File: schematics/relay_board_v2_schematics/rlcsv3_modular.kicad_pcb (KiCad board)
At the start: 2 copper layers, 45 x 75 mm, 43 parts, among them J1 Programming Header, P1 ACT_PWR, P3 ACTUATOR, Q1 MMBF170, Q2 MMBF170, SW1 SW_DIP_x04, U1 SPST_POWER_RELAY, U2 PIC16F1826-ISO, U3 dpdt_relay, U4 INA180A1, U5 CONN_01x05, U6 INA180A1, U7 CONN_01x05

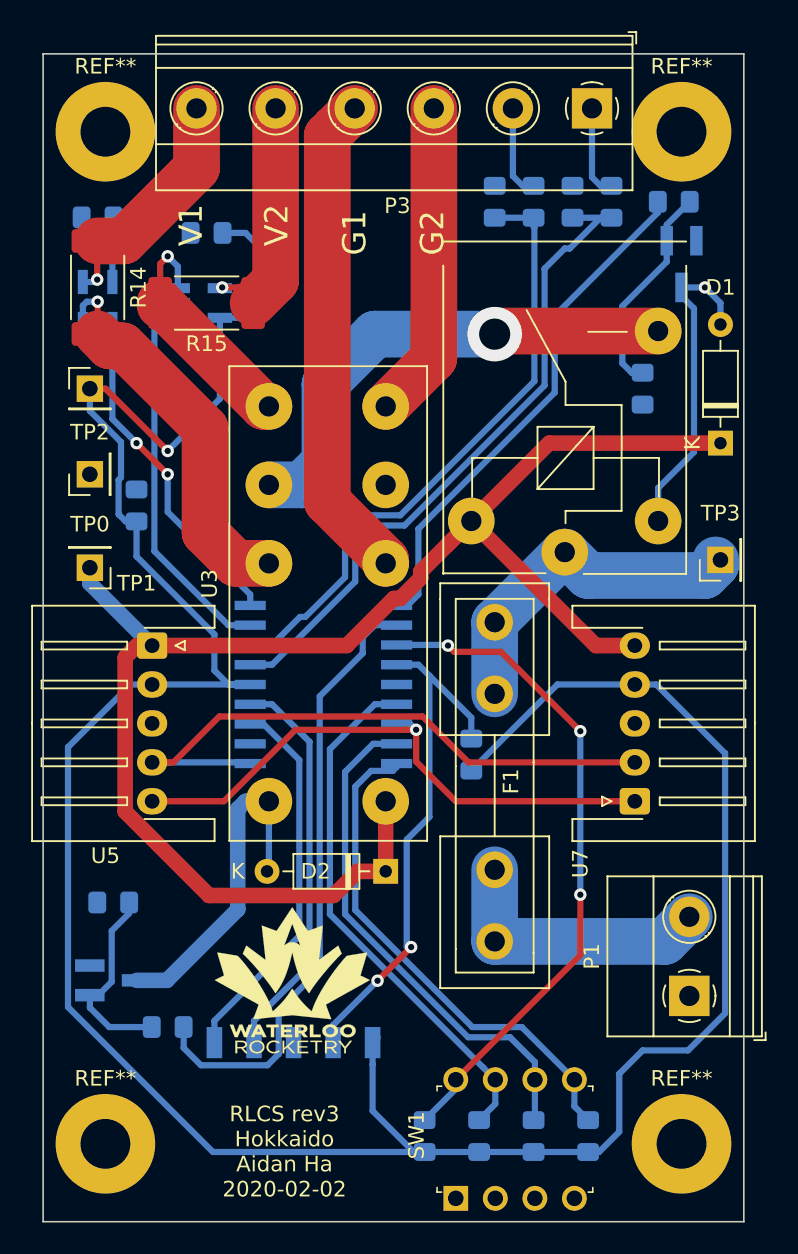
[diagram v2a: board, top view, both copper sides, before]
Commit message: Fix comments, add ground pour and DRC check changes
Signed-off-by: AIDAN HA <qbha@edu.uwaterloo.ca>
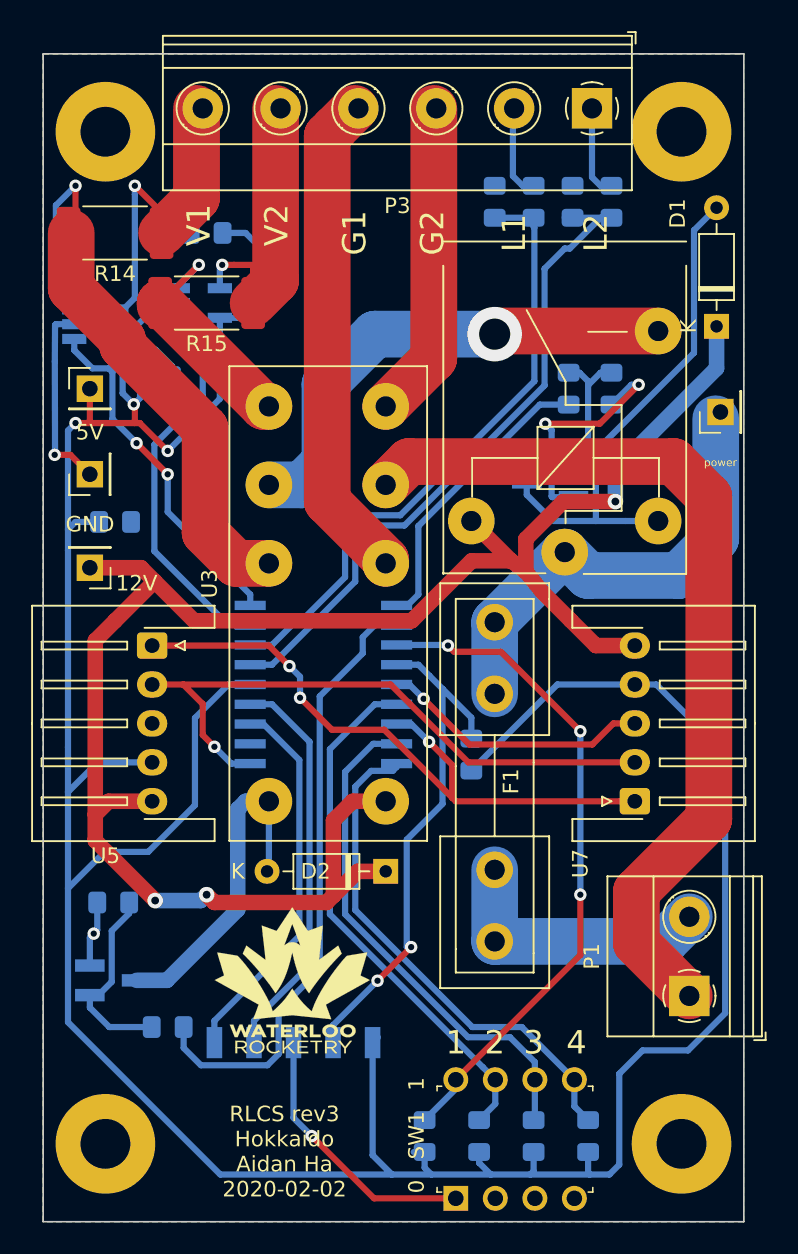
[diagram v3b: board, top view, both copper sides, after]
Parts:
- removed REF** (x2): MountingHole_3.2mm_M3_Pad, MountingHole:MountingHole_3.2mm_M3_Pad
- added ?: MountingHole_3.2mm_M3_Pad, MountingHole:MountingHole_3.2mm_M3_Pad, F.Cu at (134.0, 139.0)
- added ?: MountingHole_3.2mm_M3_Pad, MountingHole:MountingHole_3.2mm_M3_Pad, F.Cu at (171.0, 139.0)
- 0   SW1   1: renamed from SW1
- P3: footprint TerminalBlock_Phoenix:TerminalBlock_Phoenix_MKDS-1,5-6-5.08_1x06_P5.08mm_Horizontal -> TerminalBlock_Phoenix:TerminalBlock_Phoenix_MKDS-1,5-6_1x06_P5.00mm_Horizontal
- moved Q1 16.4 mm to (162.6, 96.5), turned to 180 degrees
- moved R5 13.8 mm to (163.8, 90.5), turned to 270 degrees
- moved C2 10.9 mm to (137.2, 89.8), turned to 180 degrees
- moved power 9.50 mm to (173.5, 92.0)
- moved D1 7.50 mm to (173.2, 86.5)
- moved R14 3.67 mm to (134.6, 80.5), turned to 180 degrees
- moved R11 2.00 mm to (166.5, 90.5)
- moved C1 1.74 mm to (134.6, 99.1), turned to 0 degrees
- moved U4 1.37 mm to (133.3, 86.4), turned to 0 degrees
- renumbered TP1 to 12V, TP2 to 5V, REF** to ?, TP0 to GND, TP3 to power
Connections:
- U2 pad 11: (no net) -> Net-(U2-Pad11)
- U5 pad 1: +12V -> /SDA
- U5 pad 2: +5V -> /SCL
- U5 pad 4: /SCL -> +5V
- U5 pad 5: /SDA -> +12V
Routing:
- net GND: track 0.00 -> 137.1 mm, vias 0 -> 6
- net +5V: track 183.3 -> 211.4 mm, vias 1 -> 3
- net +12V: track 100.8 -> 119.0 mm, vias 0 -> 3
- net Net-(R14-Pad2): track 25.3 -> 40.2 mm
- net /POWER: track 33.3 -> 19.0 mm
- net Net-(D1-Pad2): track 20.6 -> 33.3 mm, vias 1 -> 0
- net Net-(F1-Pad2): track 23.1 -> 31.2 mm
- net /P1: track 15.6 -> 21.4 mm
- net /SDA: track 38.4 -> 43.7 mm, vias 1 -> 3
- net Net-(Q1-Pad1): track 13.7 -> 9.24 mm
- net /P2: track 15.7 -> 19.1 mm
- net /SCL: track 39.9 -> 40.8 mm, vias 0 -> 1
- net /CURR_SENSE_1: track 21.7 -> 22.4 mm
- net /CURR_SENSE_2: track 24.4 -> 25.1 mm
- added copper zone on B.Cu, net GND
- added copper zone on F.Cu, net GND
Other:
- board text added: "1"
- board text added: "2"
- board text added: "3"
- board text added: "4"
- board text added: "L1"
- board text added: "L2"

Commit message: Add round 3 of changes
Signed-off-by: AIDAN HA <qbha@edu.uwaterloo.ca>
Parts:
- added P1: ACT_PWR, TerminalBlock_Phoenix:TerminalBlock_Phoenix_MKDS-1,5-2-5.08_1x02_P5.08mm_Horizontal, F.Cu at (135.0, 123.8)
- moved R12 8.31 mm to (137.5, 131.2)
- moved Q2 7.16 mm to (141.0, 125.5)
- moved R8 2.46 mm to (156.8, 79.5)
- moved R9 2.45 mm to (168.8, 79.5)
- moved R6 2.06 mm to (137.5, 133.5), turned to 180 degrees
- moved P1 1.90 mm to (169.8, 128.8)
- moved U4 1.42 mm to (133.8, 85.0)
- moved R10 1.25 mm to (164.8, 79.5)
- moved R7 1.25 mm to (160.8, 79.5)
- turned C1 to 180 degrees
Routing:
- net GND: track 137.1 -> 190.1 mm
- net Net-(F1-Pad1): track 17.8 -> 50.2 mm
- net +5V: track 211.4 -> 224.9 mm
- net Net-(D2-Pad2): track 23.0 -> 16.1 mm
- net /SDA: track 43.7 -> 39.1 mm
- net /SELECT: track 39.7 -> 43.2 mm
- net Net-(Q2-Pad1): track 12.6 -> 9.28 mm
- net /LIM1: track 39.7 -> 42.8 mm
- net Net-(R14-Pad2): track 40.2 -> 37.6 mm
- net Net-(P3-Pad1): track 5.90 -> 7.81 mm
- net /P1: track 21.4 -> 19.6 mm
- net /~MCLR: track 33.6 -> 34.9 mm
- net /DIP_1: track 43.2 -> 41.9 mm
- net +12V: track 119.0 -> 119.7 mm
- net /CURR_SENSE_1: track 22.4 -> 23.0 mm

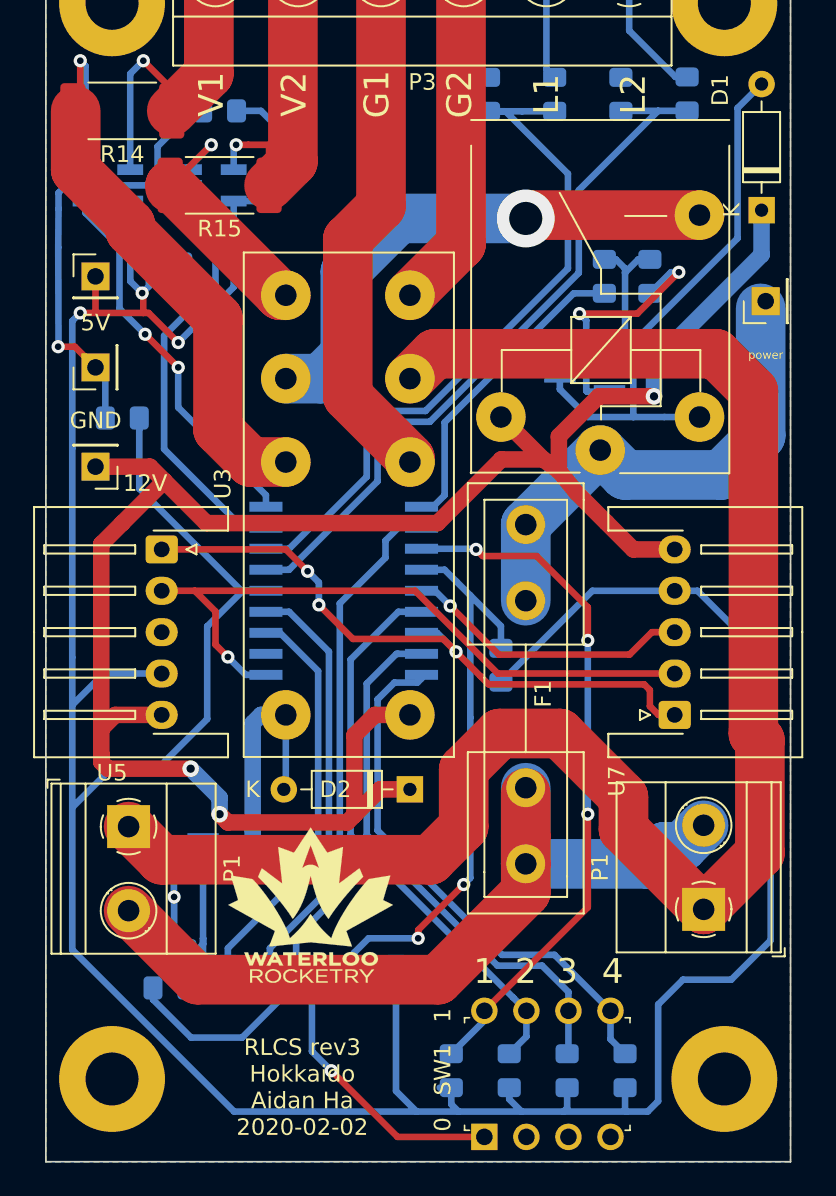
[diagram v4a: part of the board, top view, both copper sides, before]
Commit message: Add final silkscreen changes
Signed-off-by: AIDAN HA <qbha@edu.uwaterloo.ca>
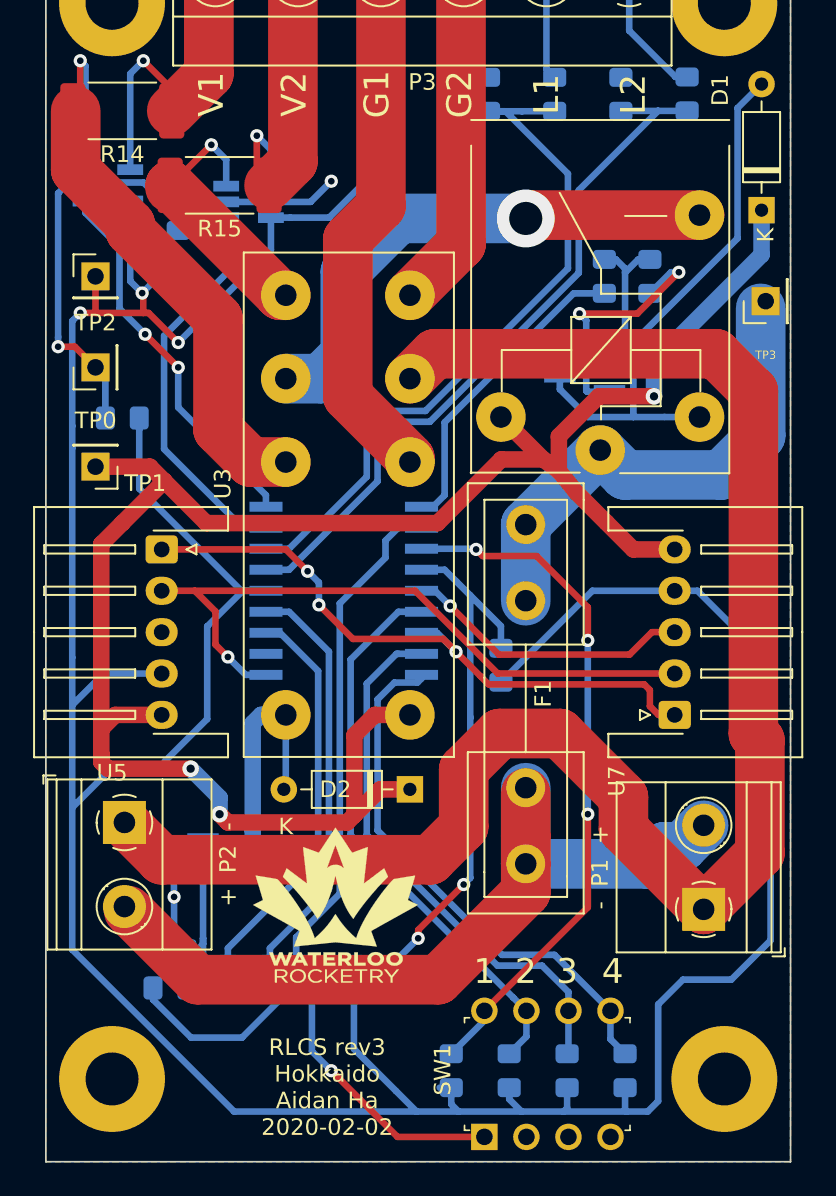
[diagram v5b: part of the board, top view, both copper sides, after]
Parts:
- removed P1: ACT_PWR, TerminalBlock_Phoenix:TerminalBlock_Phoenix_MKDS-1,5-2-5.08_1x02_P5.08mm_Horizontal
- added +  P2  -: ACT_PWR, TerminalBlock_Phoenix:TerminalBlock_Phoenix_MKDS-1,5-2-5.08_1x02_P5.08mm_Horizontal, F.Cu at (134.8, 123.5)
- -  P1  +: renamed from P1
- SW1: renamed from 0   SW1   1
- ~MCLR 5V: renamed from J1
- moved C3 9.33 mm to (149.5, 83.0), turned to 270 degrees
- moved U6 2.46 mm to (142.2, 86.0)
- moved G*** 1.50 mm to (147.5, 128.5)
- moved C2 1.25 mm to (138.0, 88.8), turned to 270 degrees
- renumbered GND to TP0, 12V to TP1, 5V to TP2, power to TP3
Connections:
- ~MCLR 5V pad 4: /~MCLR -> +5V
- ~MCLR 5V pad 5: +5V -> /~MCLR
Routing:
- net /~MCLR: track 34.9 -> 32.1 mm
- net GND: track 190.1 -> 192.1 mm, vias 6 -> 7
- net /CURR_SENSE_2: track 25.1 -> 23.7 mm
- net Net-(R15-Pad2): track 15.5 -> 16.3 mm
- net /P2: track 19.1 -> 19.8 mm

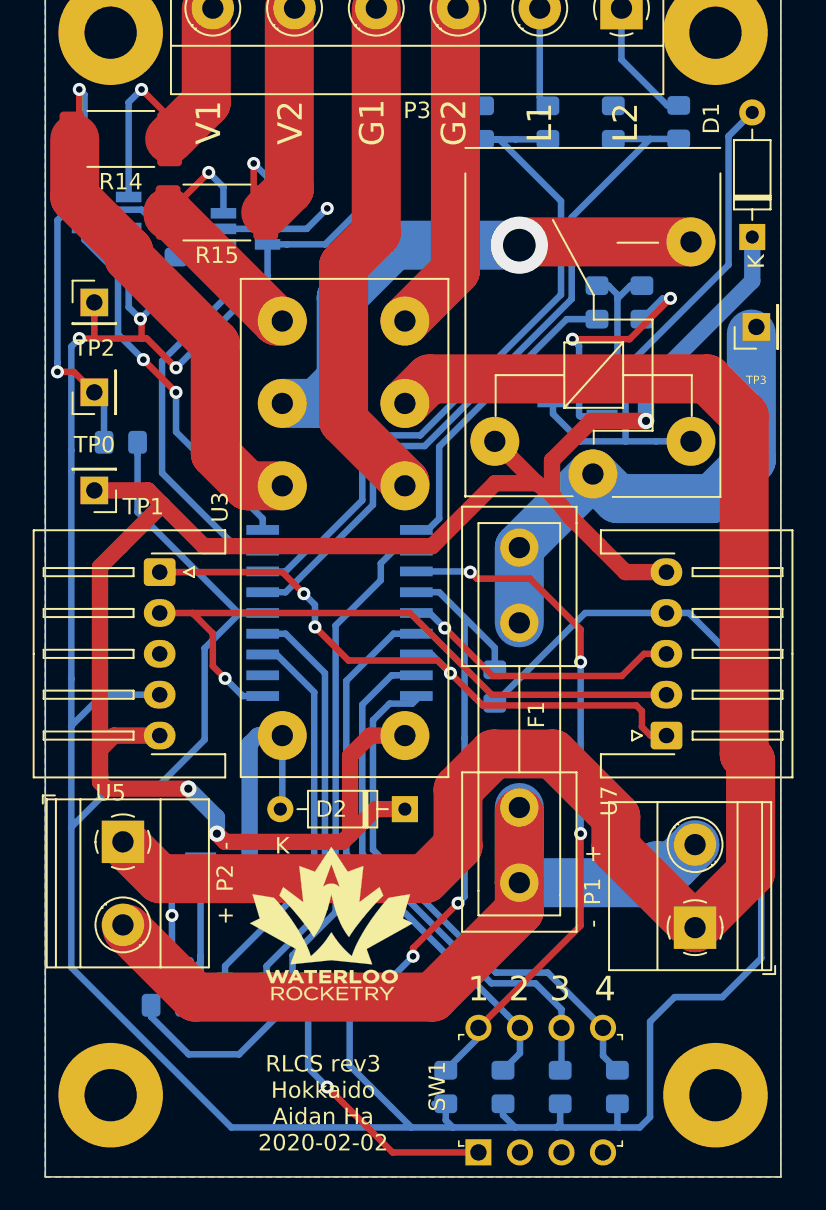
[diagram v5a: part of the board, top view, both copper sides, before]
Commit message: Fix SilkScreen and add Gerbers
Signed-off-by: AIDAN HA <qbha@edu.uwaterloo.ca>
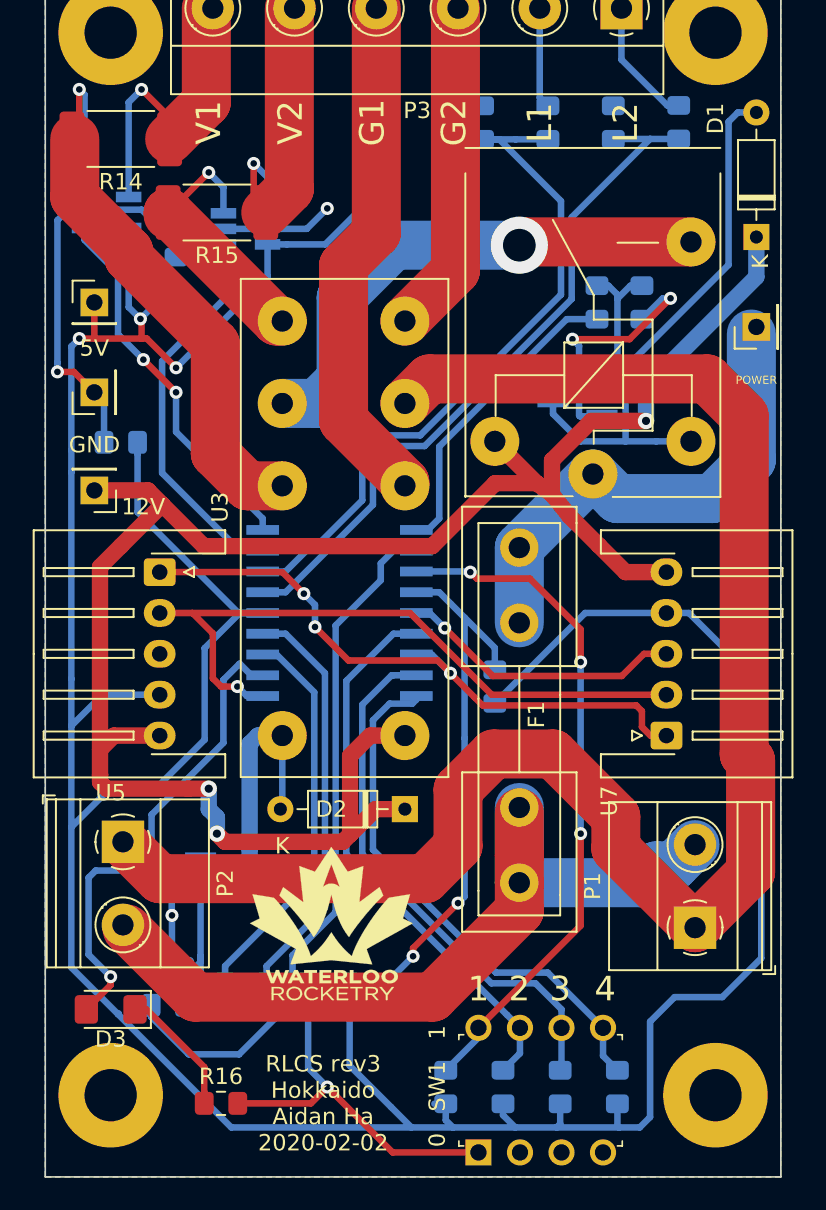
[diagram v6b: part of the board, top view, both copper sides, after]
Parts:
- added D3: D, LED_SMD:LED_1206_3216Metric_Pad1.42x1.75mm_HandSolder, F.Cu at (134.0, 133.8)
- added R16: R, Resistor_SMD:R_0805_2012Metric_Pad1.15x1.40mm_HandSolder, F.Cu at (140.8, 139.5)
- 0   SW1   1: renamed from SW1
- J1: renamed from ~MCLR 5V
- P1: renamed from -  P1  +
- P2: renamed from +  P2  -
- moved D1 0.25 mm to (173.5, 86.5)
- renumbered TP1 to 12V, TP2 to 5V, TP0 to GND, TP3 to POWER
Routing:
- net Net-(D3-Pad2): track 0.00 -> 29.8 mm, vias 0 -> 1
- net Net-(D3-Pad1): track 0.00 -> 7.92 mm
- net GND: track 192.1 -> 198.0 mm
- net +12V: track 119.7 -> 120.5 mm
- net Net-(D1-Pad2): track 33.3 -> 34.0 mm
